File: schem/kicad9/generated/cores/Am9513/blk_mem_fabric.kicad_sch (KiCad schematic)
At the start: 0 parts

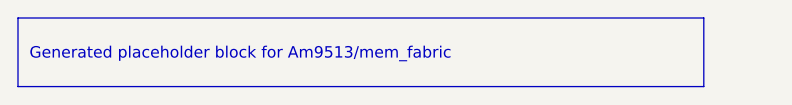
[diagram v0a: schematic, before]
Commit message: kicad: generate core-level hierarchical schematics
Detailed description:
- What changed: regenerated common and core schematics for Z85/Z90/Z380/Z480, Am9513/4/5, Am95xx, and CarbonIO/DMA placeholders
- Why it changed: update generated KiCad 9 outputs to reflect the final naming and tier model
- Files/paths affected: schem/kicad9/generated/common/* and schem/kicad9/generated/cores/*
- How to run it: scripts/gen_kicad.sh (or python tools/kicadgen/src/kicadgen.py)
- What remains TODO: regenerate and commit system-level schematics
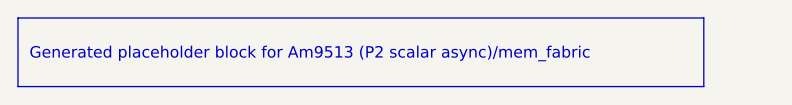
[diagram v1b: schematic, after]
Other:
- title: Am9513::mem_fabric -> Am9513 (P2 scalar async)::mem_fabric
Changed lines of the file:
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@@
 	(version 20250114)
 	(generator "kicadgen")
-	(generator_version "0.1")
+	(generator_version "0.2")
 	(paper "A3")
 	(title_block
-		(title "Am9513::mem_fabric")
+		(title "Am9513 (P2 scalar async)::mem_fabric")
 		(company "Project Carbon")
 		(comment 1 "Generated - do not edit in generated/")
@@
 	)
 	(text_box
-		"Generated placeholder block for Am9513/mem_fabric"
+		"Generated placeholder block for Am9513 (P2 scalar async)/mem_fabric"
 		(exclude_from_sim no)
 		(at
